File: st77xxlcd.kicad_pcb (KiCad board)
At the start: 2 copper layers, 100 x 60 mm, 6 parts, among them J1 Conn_01x40_MountingPin, J2 Conn_01x06_MountingPin, J3 Conn_01x24_MountingPin, J4 Conn_02x20_Counter_Clockwise, J5 Conn_01x06_Pin, J6 Conn_01x24_Pin

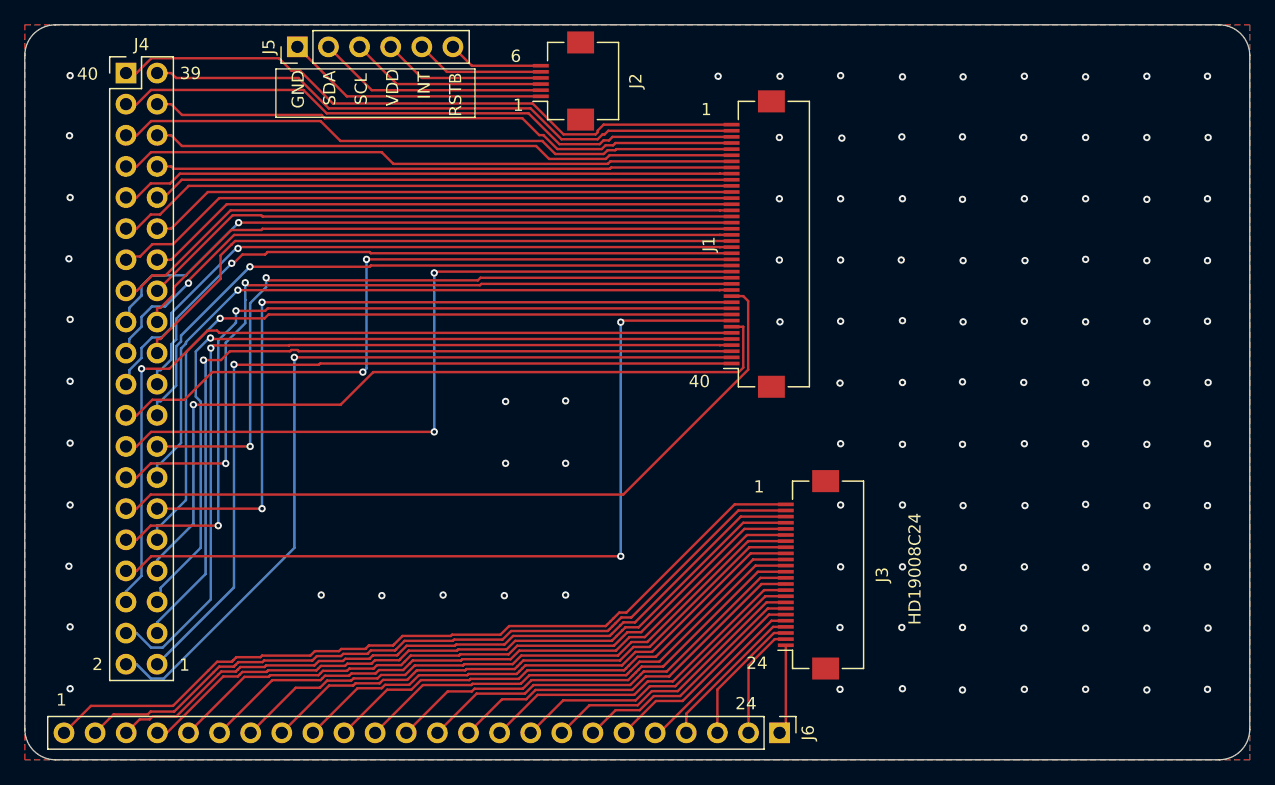
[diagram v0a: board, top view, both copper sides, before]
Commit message: [IMP] 完成布线，导出制造文件
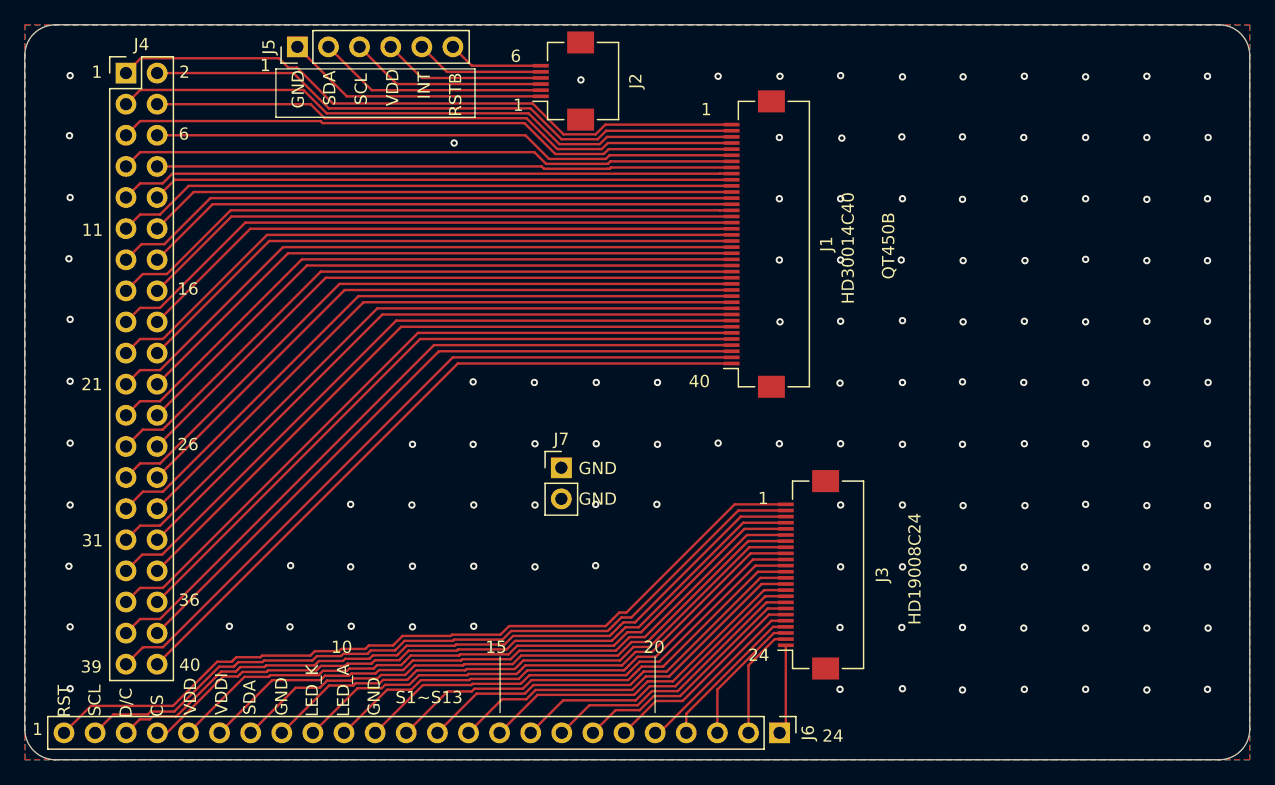
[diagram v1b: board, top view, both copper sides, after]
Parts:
- added J7: Conn_01x02_Pin, Connector_PinHeader_2.54mm:PinHeader_1x02_P2.54mm_Vertical, F.Cu at (112.2, 102.0)
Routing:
- net Net-(J1-Pin_4): track 72.2 -> 59.2 mm, vias 1 -> 0
- net Net-(J1-Pin_8): track 69.1 -> 57.9 mm, vias 2 -> 0
- net Net-(J1-Pin_3): track 67.5 -> 56.4 mm, vias 1 -> 0
- net Net-(J1-Pin_1): track 67.7 -> 57.1 mm, vias 1 -> 0
- net Net-(J1-Pin_6): track 69.1 -> 58.5 mm, vias 1 -> 0
- net Net-(J1-Pin_5): track 66.3 -> 56.2 mm, vias 1 -> 0
- net Net-(J1-Pin_2): track 69.9 -> 59.8 mm, vias 1 -> 0
- net Net-(J1-Pin_7): track 65.2 -> 55.2 mm, vias 1 -> 0
- net Net-(J1-Pin_11): track 63.7 -> 53.9 mm, vias 2 -> 0
- net Net-(J1-Pin_10): track 66.7 -> 57.3 mm, vias 2 -> 0
- net Net-(J1-Pin_14): track 63.9 -> 56.0 mm, vias 2 -> 0
- net Net-(J1-Pin_9): track 62.3 -> 54.5 mm, vias 1 -> 0
- net Net-(J1-Pin_16): track 63.0 -> 55.4 mm, vias 2 -> 0
- net Net-(J1-Pin_15): track 60.1 -> 52.6 mm, vias 2 -> 0
- net Net-(J1-Pin_12): track 62.6 -> 56.6 mm
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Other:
- board text added: "10"
- board text added: "11"
- board text added: "15"
- board text added: "16"
- board text added: "20"
- board text added: "21"
- board text added: "26"
- board text added: "31"
- board text added: "36"
- board text added: "CS"
- board text added: "D/C"
- board text added: "HD30014C40"
- board text added: "LED_A"
- board text added: "LED_K"
- board text added: "QT450B"
- board text added: "RST"
- board text added: "S1~S13"
- board text added: "VDDI"
